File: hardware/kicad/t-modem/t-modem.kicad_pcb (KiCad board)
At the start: 2 copper layers, 190 x 110 mm, 43 parts, among them Q1 2N2222A, SW1 BOOTSEL, U1 RaspberryPi_Pico, Y1 4.433619

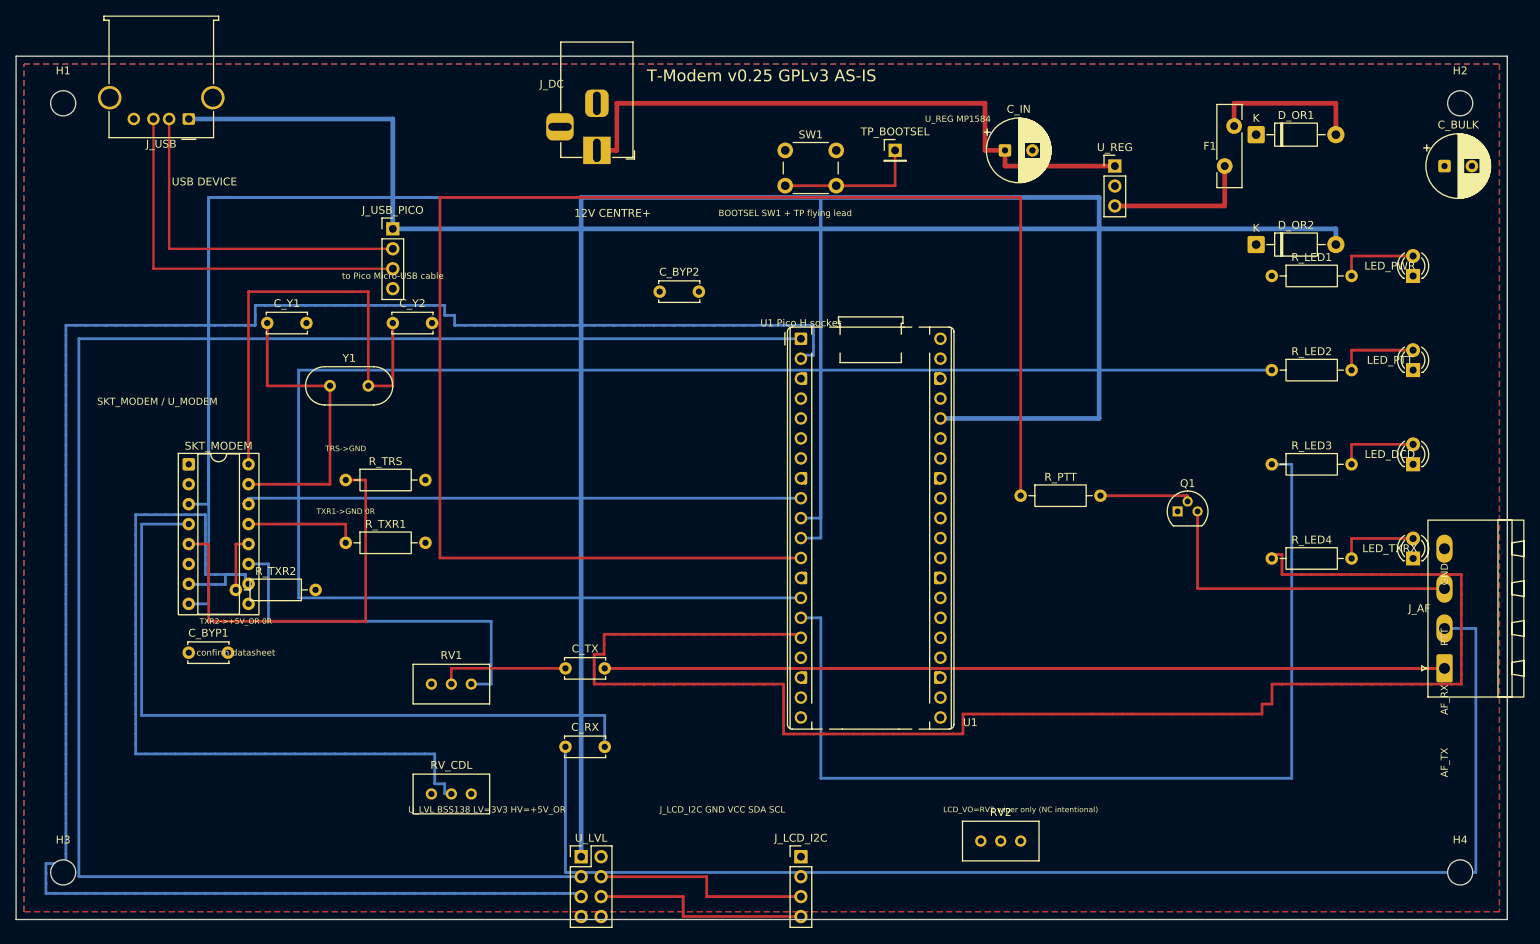
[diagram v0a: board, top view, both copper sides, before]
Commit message: v0.25-pcb-ready-for-prototype
Promote routed copper board to t-modem.kicad_pcb (DRC short/unconn/cross 0/0/0); drop workcopies and Freerouting artifacts from the tree.

Co-authored-by: Cursor <cursoragent@cursor.com>
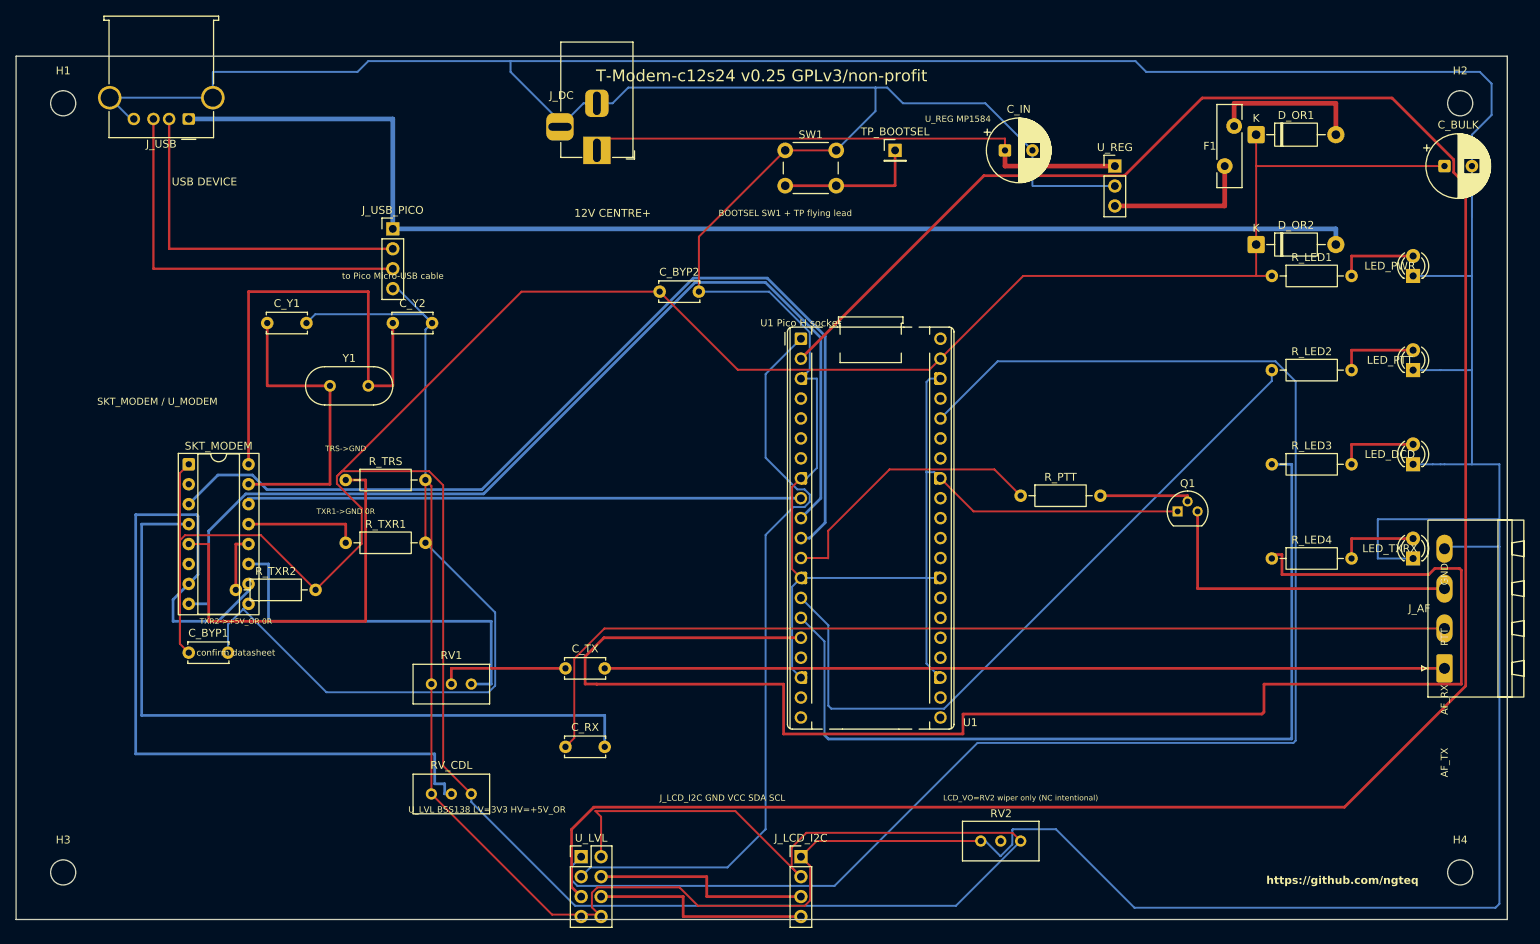
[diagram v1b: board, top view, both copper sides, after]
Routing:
- net GND: track 0.00 -> 969.2 mm
- net +5V_OR: track 0.00 -> 462.4 mm
- net PTT_DRV: track 203.9 -> 36.1 mm
- net I2C_SDA_3V3: track 224.5 -> 96.4 mm
- net LED_PTT_N: track 217.0 -> 90.5 mm
- net AF_TX: track 214.0 -> 107.0 mm
- net I2C_SCL_3V3: track 250.5 -> 299.6 mm
- net MODEM_RXD: track 175.7 -> 129.9 mm
- net AF_RX: track 167.1 -> 124.2 mm, vias 2 -> 1
- net MODEM_CDT: track 165.6 -> 125.3 mm
- net LED_DCD_N: track 125.5 -> 113.5 mm
- net VIN_12: track 80.0 -> 70.1 mm
- net CDL: track 111.1 -> 112.8 mm, vias 4 -> 3
- net VBUS: vias 4 -> 3
- removed copper zone on F.Cu, net +5V_OR
- removed copper zone on B.Cu, net GND
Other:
- board text added: "T-Modem-c12s24 v0.25 GPLv3/non-profit"
- board text added: "https://github.com/ngteq"
- board text removed: "T-Modem v0.25 GPLv3 AS-IS"

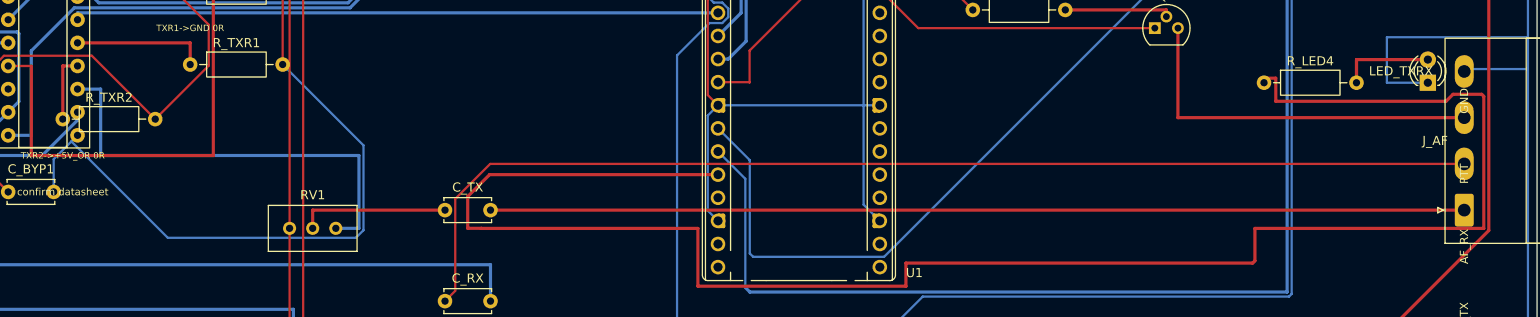
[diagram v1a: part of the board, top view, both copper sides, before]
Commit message: fix(pcb): restore copper clearances before fab etch risk
LED_TXRX_N↔AF_TX and CDL↔TXR2_N were under 0.2 mm; nudge stubs so DRC clearance is clean while keeping short/unconn/cross at 0.

Co-authored-by: Cursor <cursoragent@cursor.com>
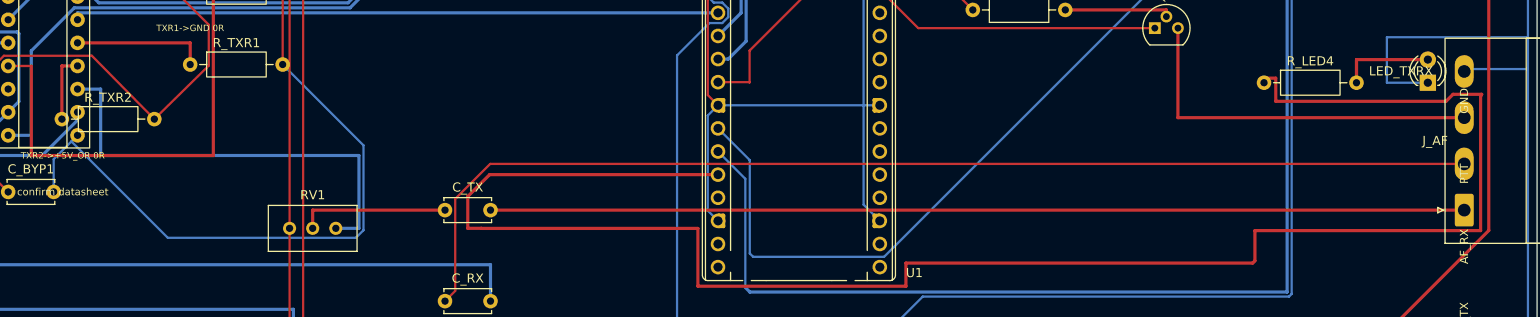
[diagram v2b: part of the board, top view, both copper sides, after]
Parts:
- moved R_TXR2 0.10 mm to (27.9, 68.0)
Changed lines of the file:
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@@
 	(footprint "R_Axial_DIN0207_L6.3mm_D2.5mm_P10.16mm_Horizontal"
 		(layer "F.Cu")
-		(at 28 68)
+		(at 27.9 68)
 		(descr "Resistor, Axial_DIN0207 series, Axial, Horizontal, pin pitch=10.16mm, 0.25W = 1/4W, length*diameter=6.3*2.5mm^2, http://cdn-reichelt.de/documents/datenblatt/B400/1_4W%23YAG.pdf")
 		(tags "Resistor Axial_DIN0207 series Axial Horizontal pin pitch 10.16mm 0.25W = 1/4W length 6.3mm diameter 2.5mm")
@@
 	)
 	(segment
-		(start 38.16 68)
+		(start 38.06 68)
 		(end 31.195 61.035)
 		(width 0.25)
@@
 	)
 	(segment
-		(start 38.16 68)
+		(start 38.06 68)
 		(end 44.04 62.12)
 		(width 0.25)
@@
 	)
 	(segment
-		(start 28 62.16)
-		(end 28 68)
+		(start 27.9 62.16)
+		(end 27.9 68)
 		(width 0.35)
 		(layer "F.Cu")
@@
 	(segment
 		(start 29.62 62.16)
-		(end 28 62.16)
+		(end 27.9 62.16)
 		(width 0.35)
 		(layer "F.Cu")
@@
 	(segment
 		(start 183.92 65.27)
-		(end 184.15 65.5)
+		(end 183.8 65.5)
 		(width 0.35)
 		(layer "F.Cu")
@@
 	)
 	(segment
-		(start 184.15 65.5)
-		(end 184.15 80.01)
+		(start 183.8 65.5)
+		(end 183.8 80.25)
 		(width 0.35)
 		(layer "F.Cu")
@@
 	)
 	(segment
-		(start 184.15 80.01)
-		(end 159 80.01)
+		(start 183.8 80.25)
+		(end 159 80.25)
 		(width 0.35)
 		(layer "F.Cu")
@@
 	)
 	(segment
-		(start 159 80.01)
+		(start 159 80.25)
 		(end 159 83.57)
 		(width 0.35)

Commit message: fix(pcb): pull U_LVL and J_LCD_I2C on-board at bottom edge
Bottom-row pads/vias sat on Edge.Cuts (y≈109.62); move footprints
inward 0.55 mm so copper is fully on-board without breaking routing.

Co-authored-by: Cursor <cursoragent@cursor.com>
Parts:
- moved J_LCD_I2C 0.55 mm to (100.0, 101.5)
- moved U_LVL 0.55 mm to (72.0, 101.5)
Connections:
- R_TRS pad 2: GND -> MODEM_CLK
- R_TXR2 pad 2: +5V_OR -> GND
- SKT_MODEM pad 2: (no net) -> MODEM_CLK
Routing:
- net MODEM_CLK: track 0.00 -> 79.6 mm
- net +5V_OR: track 462.4 -> 499.4 mm
- net TRS_N: track 52.9 -> 23.4 mm
- net GND: track 969.2 -> 977.0 mm, vias 37 -> 36
- net I2C_SCL_5V: track 28.0 -> 26.7 mm
- net CDL: track 112.8 -> 112.0 mm
- net TXR1_N: track 14.8 -> 15.5 mm
- net I2C_SCL_3V3: track 299.6 -> 299.1 mm
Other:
- board text added: "TRS_N-> M_CLK"
- board text added: "TXR2-> GND"
- board text removed: "TRS->GND"
- board text removed: "TXR2->+5V_OR 0R"
